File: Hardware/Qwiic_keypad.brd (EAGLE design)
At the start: 25.4 x 25.4 mm, 36 parts, among them J3 PTH, J6 AVR_SPI_PROG_3X2TESTPOINTS, U3 ATTINY84

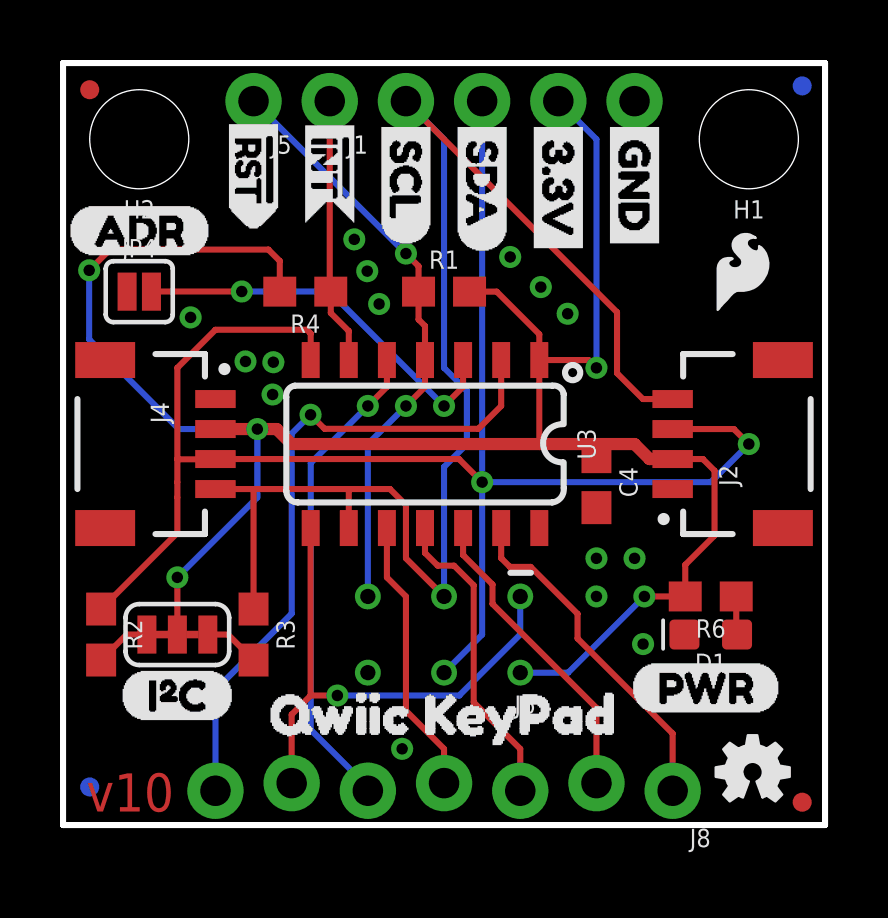
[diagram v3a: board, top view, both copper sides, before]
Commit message: hardware review changes
beef up trace to 3.3V PTH header breakout as well.
Nudged I2C label up to match power label hieght.
ATTINY84 polarity mark fill in library
Logo up to .2 size flame.
Schematic note for I2C pullup jumper
Updated ATTiny device (just the symbol changed, but needed to "replace" due to new pin names).
nudged LED lower to ensure mask gap from nearby resistor
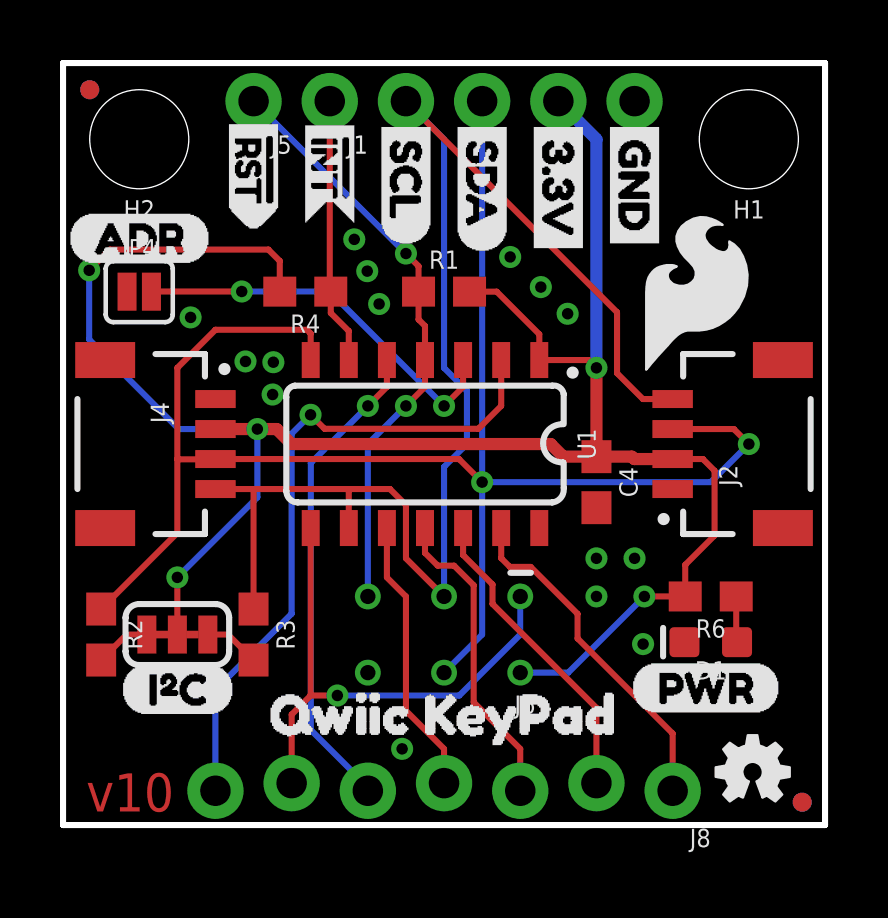
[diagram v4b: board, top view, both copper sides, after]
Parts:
- added LOGO2: SFE_LOGO_NAME_FLAME.1_INCH, SparkFun-Aesthetics:SFE_LOGO_NAME_FLAME_.1
- LOGO3: value SFE_LOGO_FLAME.1_INCH -> SFE_LOGO_FLAME.2_INCH; device SparkFun-Aesthetics:SFE_LOGO_FLAME_.1 -> SparkFun-Aesthetics:SFE_LOGO_FLAME_.2
- moved JP3 23.9 mm to (24.6, 0.76)
- moved JP1 23.2 mm to (0.89, 24.5)
- moved LOGO3 1.70 mm to (21.1, 17.7)
- moved U$10 0.25 mm to (0.13, 19.6)
- moved D1 0.25 mm to (21.6, 6.10)
- moved U$9 0.20 mm to (1.92, 4.52)
- renumbered SJ5 to I2C, U3 to U1

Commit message: double-check (my run) fixes
added SS path on 48.
package update on address jumper - to 8 mil width on silk outline.
library update to SFE library on I2C jumper (was sparkx lbr).
some minor routing tweaks to allow more gnd flow
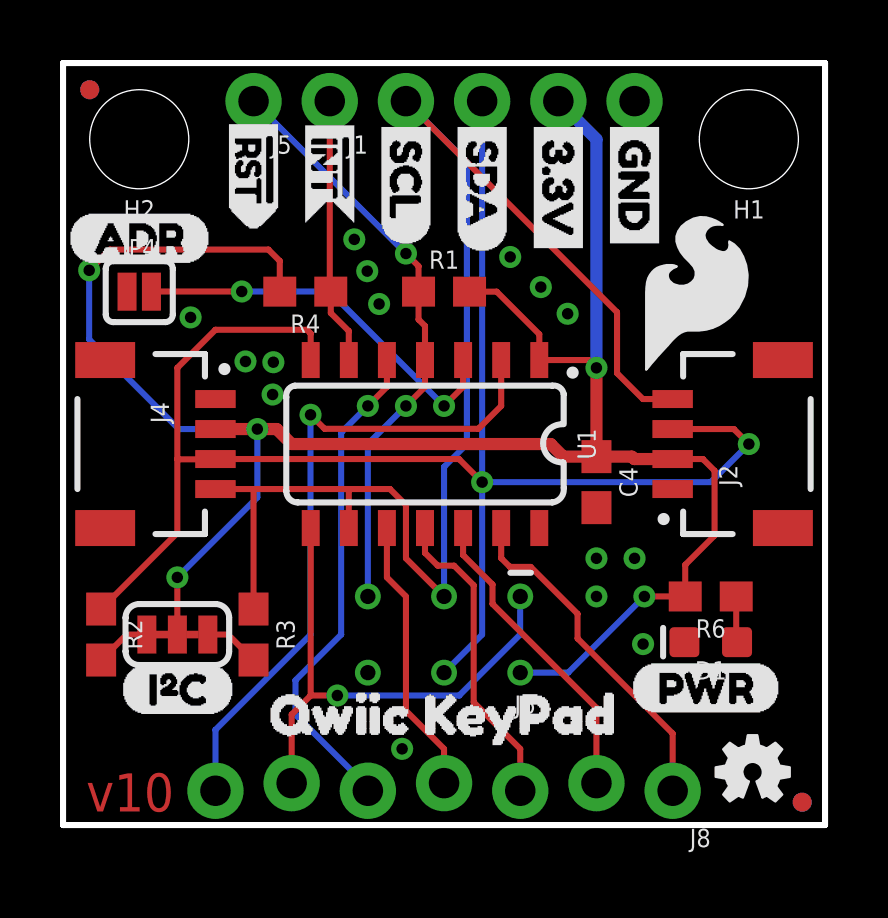
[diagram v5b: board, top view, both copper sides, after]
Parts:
- J3: device SparkX:1X04_NO_SILK -> SparkFun-Connectors:1X04_NO_SILK
- JP4: value (none) -> JUMPER-SMT_2_NO_SILK
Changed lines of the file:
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@@
 <layer number="18" name="Vias" color="2" fill="1" visible="yes" active="yes"/>
 <layer number="19" name="Unrouted" color="6" fill="1" visible="yes" active="yes"/>
-<layer number="20" name="Dimension" color="15" fill="1" visible="yes" active="yes"/>
-<layer number="21" name="tPlace" color="16" fill="1" visible="yes" active="yes"/>
-<layer number="22" name="bPlace" color="14" fill="1" visible="yes" active="yes"/>
-<layer number="23" name="tOrigins" color="15" fill="1" visible="yes" active="yes"/>
-<layer number="24" name="bOrigins" color="15" fill="1" visible="yes" active="yes"/>
+<layer number="20" name="Dimension" color="15" fill="1" visible="no" active="yes"/>
+<layer number="21" name="tPlace" color="16" fill="1" visible="no" active="yes"/>
+<layer number="22" name="bPlace" color="14" fill="1" visible="no" active="yes"/>
+<layer number="23" name="tOrigins" color="15" fill="1" visible="no" active="yes"/>
+<layer number="24" name="bOrigins" color="15" fill="1" visible="no" active="yes"/>
 <layer number="25" name="tNames" color="7" fill="1" visible="no" active="yes"/>
 <layer number="26" name="bNames" color="7" fill="1" visible="no" active="yes"/>
@@
 <layer number="43" name="vRestrict" color="2" fill="10" visible="no" active="yes"/>
 <layer number="44" name="Drills" color="7" fill="1" visible="no" active="yes"/>
-<layer number="45" name="Holes" color="7" fill="1" visible="yes" active="yes"/>
-<layer number="46" name="Milling" color="3" fill="1" visible="yes" active="yes"/>
+<layer number="45" name="Holes" color="7" fill="1" visible="no" active="yes"/>
+<layer number="46" name="Milling" color="3" fill="1" visible="no" active="yes"/>
 <layer number="47" name="Measures" color="7" fill="1" visible="no" active="yes"/>
-<layer number="48" name="Document" color="7" fill="1" visible="no" active="yes"/>
+<layer number="48" name="SS" color="63" fill="7" visible="no" active="yes"/>
 <layer number="49" name="Reference" color="7" fill="1" visible="no" active="yes"/>
 <layer number="50" name="dxf" color="7" fill="1" visible="no" active="yes"/>
-<layer number="51" name="tDocu" color="6" fill="1" visible="yes" active="yes"/>
+<layer number="51" name="tDocu" color="6" fill="1" visible="no" active="yes"/>
 <layer number="52" name="bDocu" color="7" fill="1" visible="no" active="yes"/>
 <layer number="53" name="tGND_GNDA" color="7" fill="9" visible="no" active="no"/>
@@
 <wire x1="0" y1="25.4" x2="25.4" y2="25.4" width="0.2032" layer="20"/>
 <text x="2.2352" y="1.08711875" size="1.27" layer="1" font="vector" ratio="15" rot="SR0" align="center">v10</text>
-<dimension x1="0" y1="25.4" x2="0" y2="0" x3="-8.89" y3="12.7" textsize="1.27" textratio="15" layer="47" unit="inch"/>
-<text x="17.78" y="-11.43" size="1.778" layer="51" font="vector" ratio="15">Kevin Kuwata</text>
+<dimension x1="0" y1="25.4" x2="0" y2="0" x3="-7.62" y3="12.7" textsize="1.27" textratio="15" layer="47" unit="inch"/>
+<text x="17.78" y="-11.43" size="1.778" layer="51" font="vector">Kevin Kuwata</text>
 <wire x1="25.4" y1="0" x2="25.4" y2="25.4" width="0.2032" layer="20"/>
-<dimension x1="0" y1="25.4" x2="30.48" y2="25.4" x3="15.24" y3="35.56" textsize="1.778" textratio="15" layer="47" unit="inch"/>
-<dimension x1="0" y1="0" x2="25.4" y2="0" x3="12.7" y3="-6.35" textsize="1.778" textratio="15" layer="47" unit="inch"/>
+<dimension x1="0" y1="25.4" x2="25.4" y2="25.4" x3="12.7" y3="35.56" textsize="1.27" textratio="15" layer="47" unit="inch"/>
 <text x="-2.54" y="-13.97" size="1.778" layer="51" font="vector">Revised by: Pete Lewis</text>
+<wire x1="5.08" y1="1.27" x2="20.32" y2="1.27" width="4.5212" layer="48"/>
+<dimension x1="0" y1="0" x2="0" y2="22.86" x3="-3.81" y3="11.43" textsize="1.27" layer="47" unit="inch"/>
+<dimension x1="0" y1="25.4" x2="22.86" y2="25.4" x3="11.43" y3="31.75" textsize="1.27" layer="47" unit="inch"/>
+<dimension x1="0" y1="25.4" x2="2.54" y2="25.4" x3="1.27" y3="27.94" textsize="1.27" layer="47" unit="inch"/>
 </plain>
 <attributes>
@@
 <attribute name="VALUE" x="23.622" y="11.049" size="0.6096" layer="27" font="vector" ratio="20" rot="R90"/>
 </element>
-<element name="J3" library="SparkX" package="1X04_NO_SILK" value="PTH" x="19.05" y="24.13" smashed="yes" rot="R180">
+<element name="J3" library="SparkFun-Connectors" package="1X04_NO_SILK" value="PTH" x="19.05" y="24.13" smashed="yes" rot="R180">
 <attribute name="VALUE" x="20.32" y="26.162" size="0.6096" layer="27" font="vector" ratio="20" rot="R180"/>
 </element>
@@
 <attribute name="VALUE" x="7.62" y="25.908" size="0.6096" layer="27" font="vector" ratio="20" rot="R180"/>
 </element>
-<element name="JP4" library="SparkFun-Jumpers" package="SMT-JUMPER_2_NO_SILK" value="" x="2.54" y="17.78" smashed="yes">
+<element name="JP4" library="SparkFun-Jumpers" package="SMT-JUMPER_2_NO_SILK" value="JUMPER-SMT_2_NO_SILK" x="2.54" y="17.78" smashed="yes">
 <attribute name="NAME" x="2.54" y="18.923" size="0.6096" layer="25" font="vector" ratio="20" align="bottom-center"/>
 <attribute name="VALUE" x="2.54" y="16.637" size="0.6096" layer="27" font="vector" ratio="20" align="top-center"/>
@@
 <via x="8.249921875" y="13.675359375" extent="1-16" drill="0.381"/>
 <wire x1="13.843" y1="13.208" x2="14.605" y2="13.97" width="0.2032" layer="1"/>
-<wire x1="7.62" y1="7.04341875" x2="7.62" y2="13.0454375" width="0.2032" layer="16"/>
 <wire x1="13.843" y1="13.208" x2="8.71728125" y2="13.208" width="0.2032" layer="1"/>
-<wire x1="5.08" y1="1.143" x2="5.08" y2="4.50341875" width="0.2032" layer="16"/>
-<wire x1="5.08" y1="4.50341875" x2="7.62" y2="7.04341875" width="0.2032" layer="16"/>
-<wire x1="7.62" y1="13.0454375" x2="8.249921875" y2="13.675359375" width="0.2032" layer="16"/>
 <wire x1="8.249921875" y1="13.675359375" x2="8.71728125" y2="13.208" width="0.2032" layer="1"/>
 <contactref element="U1" pad="2"/>
 <wire x1="14.605" y1="15.5" x2="14.605" y2="13.97" width="0.2032" layer="1"/>
+<wire x1="5.08" y1="1.143" x2="5.08" y2="3.175" width="0.2032" layer="16"/>
+<wire x1="5.08" y1="3.175" x2="8.249921875" y2="6.344921875" width="0.2032" layer="16"/>
+<wire x1="8.249921875" y1="6.344921875" x2="8.249921875" y2="13.675359375" width="0.2032" layer="16"/>
 </signal>
 <signal name="5">
@@
 <wire x1="10.795" y1="14.605" x2="10.16" y2="13.97" width="0.2032" layer="1"/>
 <via x="10.16" y="13.97" extent="1-16" drill="0.381"/>
-<wire x1="8.257540625" y1="12.067540625" x2="10.16" y2="13.97" width="0.2032" layer="16"/>
-<wire x1="8.257540625" y1="12.067540625" x2="8.257540625" y2="3.172459375" width="0.2032" layer="16"/>
-<wire x1="8.257540625" y1="3.172459375" x2="10.16" y2="1.27" width="0.2032" layer="16"/>
-<wire x1="10.16" y1="1.27" x2="10.16" y2="1.143" width="0.2032" layer="16"/>
+<wire x1="10.16" y1="1.143" x2="10.16" y2="1.27" width="0.2032" layer="16"/>
 <contactref element="U1" pad="5"/>
 <wire x1="10.795" y1="15.5" x2="10.795" y2="14.605" width="0.2032" layer="1"/>
+<wire x1="9.271" y1="6.35" x2="9.271" y2="13.081" width="0.2032" layer="16"/>
+<wire x1="9.271" y1="13.081" x2="10.16" y2="13.97" width="0.2032" layer="16"/>
+<wire x1="7.747" y1="3.683" x2="7.747" y2="4.826" width="0.2032" layer="16"/>
+<wire x1="7.747" y1="4.826" x2="9.271" y2="6.35" width="0.2032" layer="16"/>
+<wire x1="10.16" y1="1.27" x2="7.747" y2="3.683" width="0.2032" layer="16"/>
 </signal>
 <signal name="SCL">
@@
 <wire x1="12.7" y1="7.62" x2="12.7" y2="11.938" width="0.2032" layer="16"/>
 <wire x1="12.7" y1="11.938" x2="13.462" y2="12.7" width="0.2032" layer="16"/>
-<wire x1="13.462" y1="12.7" x2="13.462" y2="14.478" width="0.2032" layer="16"/>
-<wire x1="13.462" y1="14.478" x2="12.7" y2="15.24" width="0.2032" layer="16"/>
-<wire x1="12.7" y1="15.24" x2="12.7" y2="22.86" width="0.2032" layer="16"/>
-<wire x1="12.7" y1="22.86" x2="11.43" y2="24.13" width="0.2032" layer="16"/>
+<wire x1="13.462" y1="12.7" x2="13.462" y2="22.098" width="0.2032" layer="16"/>
+<wire x1="13.462" y1="22.098" x2="11.43" y2="24.13" width="0.2032" layer="16"/>
 <wire x1="20.32" y1="14.2" x2="19.328" y2="14.2" width="0.2032" layer="1"/>
 <wire x1="19.328" y1="14.2" x2="18.4658" y2="15.0622" width="0.2032" layer="1"/>
